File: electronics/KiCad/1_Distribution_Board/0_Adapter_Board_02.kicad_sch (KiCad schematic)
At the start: 16 parts, among them J7 JST PH, J8 Generic 2.54mm

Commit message: footprint additions
Added Footprints to resistors and most components.
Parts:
- R1, R36, R38, R47, R5, R6, R7, R8, R9: footprint (none) -> Resistor_SMD:R_0805_2012Metric_Pad1.20x1.40mm_HandSolder
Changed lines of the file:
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@@
 			)
 		)
-		(property "Footprint" ""
+		(property "Footprint" "Resistor_SMD:R_0805_2012Metric_Pad1.20x1.40mm_HandSolder"
 			(at 41.656 65.024 90)
 			(effects
@@
 			)
 		)
-		(property "Footprint" ""
+		(property "Footprint" "Resistor_SMD:R_0805_2012Metric_Pad1.20x1.40mm_HandSolder"
 			(at 196.596 98.044 90)
 			(effects
@@
 			)
 		)
-		(property "Footprint" ""
+		(property "Footprint" "Resistor_SMD:R_0805_2012Metric_Pad1.20x1.40mm_HandSolder"
 			(at 63.246 65.024 90)
 			(effects
@@
 			)
 		)
-		(property "Footprint" ""
+		(property "Footprint" "Resistor_SMD:R_0805_2012Metric_Pad1.20x1.40mm_HandSolder"
 			(at 60.706 161.544 90)
 			(effects
@@
 			)
 		)
-		(property "Footprint" ""
+		(property "Footprint" "Resistor_SMD:R_0805_2012Metric_Pad1.20x1.40mm_HandSolder"
 			(at 63.246 75.184 90)
 			(effects
@@
 			)
 		)
-		(property "Footprint" ""
+		(property "Footprint" "Resistor_SMD:R_0805_2012Metric_Pad1.20x1.40mm_HandSolder"
 			(at 73.406 26.924 90)
 			(effects
@@
 			)
 		)
-		(property "Footprint" ""
+		(property "Footprint" "Resistor_SMD:R_0805_2012Metric_Pad1.20x1.40mm_HandSolder"
 			(at 72.136 128.524 90)
 			(effects
@@
 			)
 		)
-		(property "Footprint" ""
+		(property "Footprint" "Resistor_SMD:R_0805_2012Metric_Pad1.20x1.40mm_HandSolder"
 			(at 196.596 87.884 90)
 			(effects
@@
 			)
 		)
-		(property "Footprint" ""
+		(property "Footprint" "Resistor_SMD:R_0805_2012Metric_Pad1.20x1.40mm_HandSolder"
 			(at 41.656 75.184 90)
 			(effects

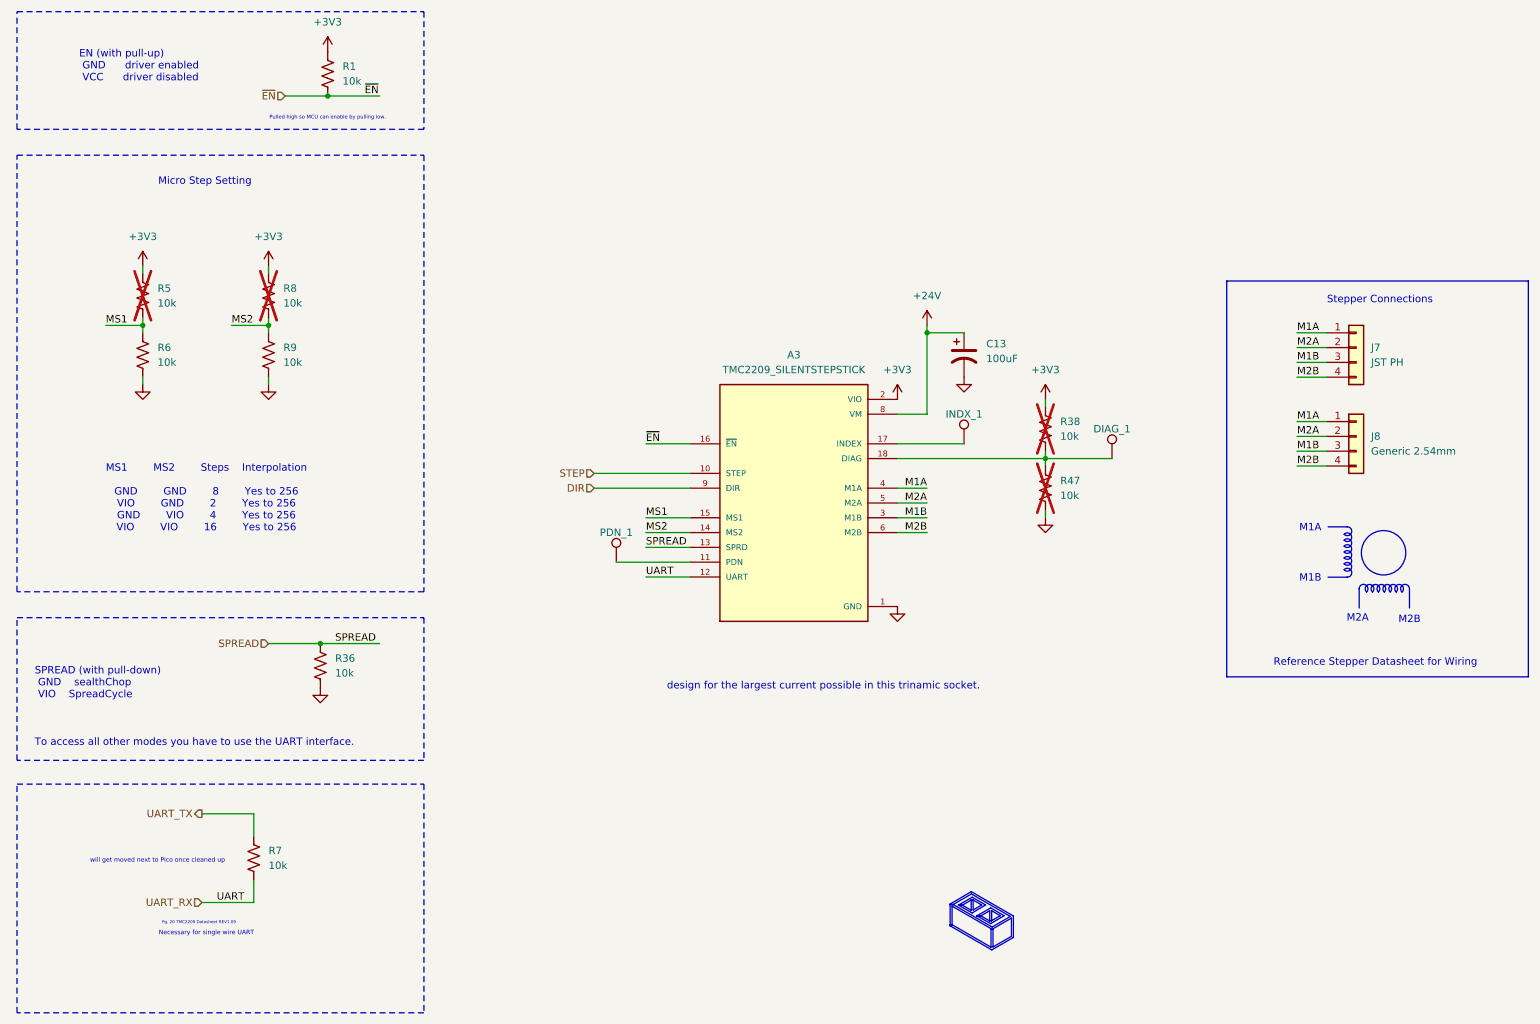
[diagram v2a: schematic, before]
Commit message: Updated to add 2 more steppers
Updated to add two more steppers, dual with the motor controllers. they will be either or. Layout hole pattern started. Still need some footprints assigned.
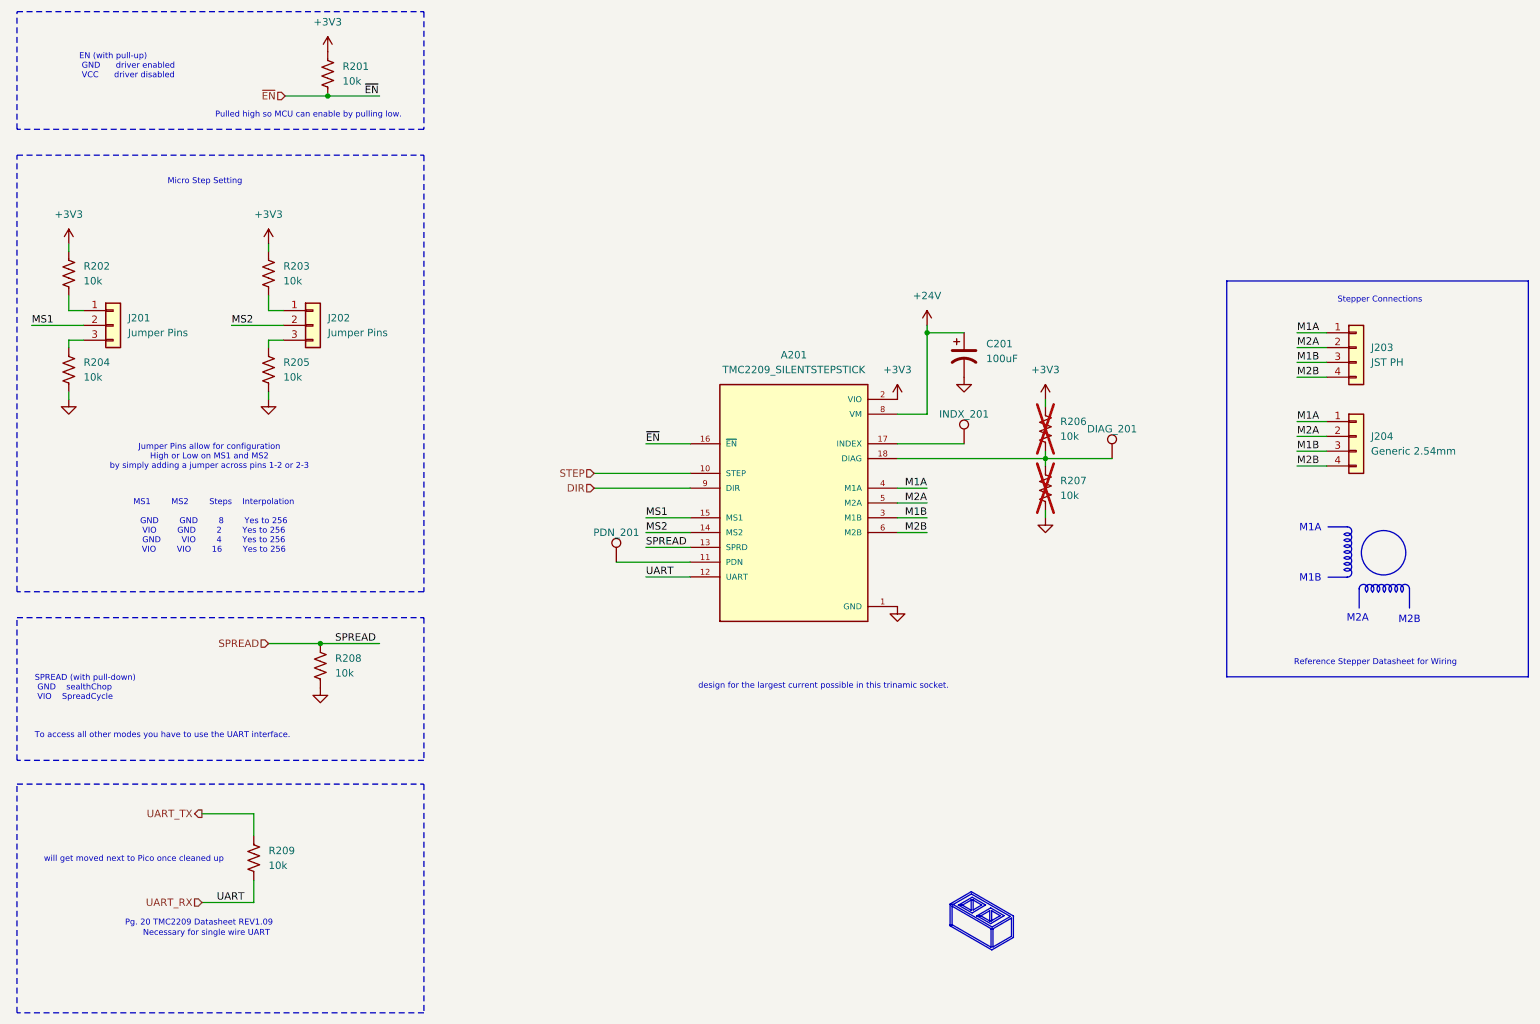
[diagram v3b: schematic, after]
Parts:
- added J201, J202: Jumper Pins, Connector_PinHeader_2.54mm:PinHeader_1x03_P2.54mm_Vertical, symbol Connector_Generic:Conn_01x03
- R202: renamed from R5; now fitted
- R203: renamed from R8; now fitted
- renumbered A3 to A201, C13 to C201, DIAG_1 to DIAG_201, INDX_1 to INDX_201, J7 to J203, J8 to J204, PDN_1 to PDN_201, R1 to R201, R6 to R204, R9 to R205, R38 to R206, R47 to R207, R36 to R208, R7 to R209
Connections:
- net MS1: now also J201.2 (Pin_2); no longer R202.2, R204.1
- net MS2: now also J202.2 (Pin_2); no longer R203.2, R205.1
- new net: J202.1 (Pin_1), R203.2
- new net: J202.3 (Pin_3), R205.1
- new net: J201.1 (Pin_1), R202.2
- new net: J201.3 (Pin_3), R204.1
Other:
- note added: "Jumper Pins allow for configuration High or Low on MS1 and MS2 by simply adding a jumper across pins 1-2 or 2-3"
- moved on the sheet: R204, R205

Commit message: Added 4th stepper
Added 4th stepper on SCH and PCB
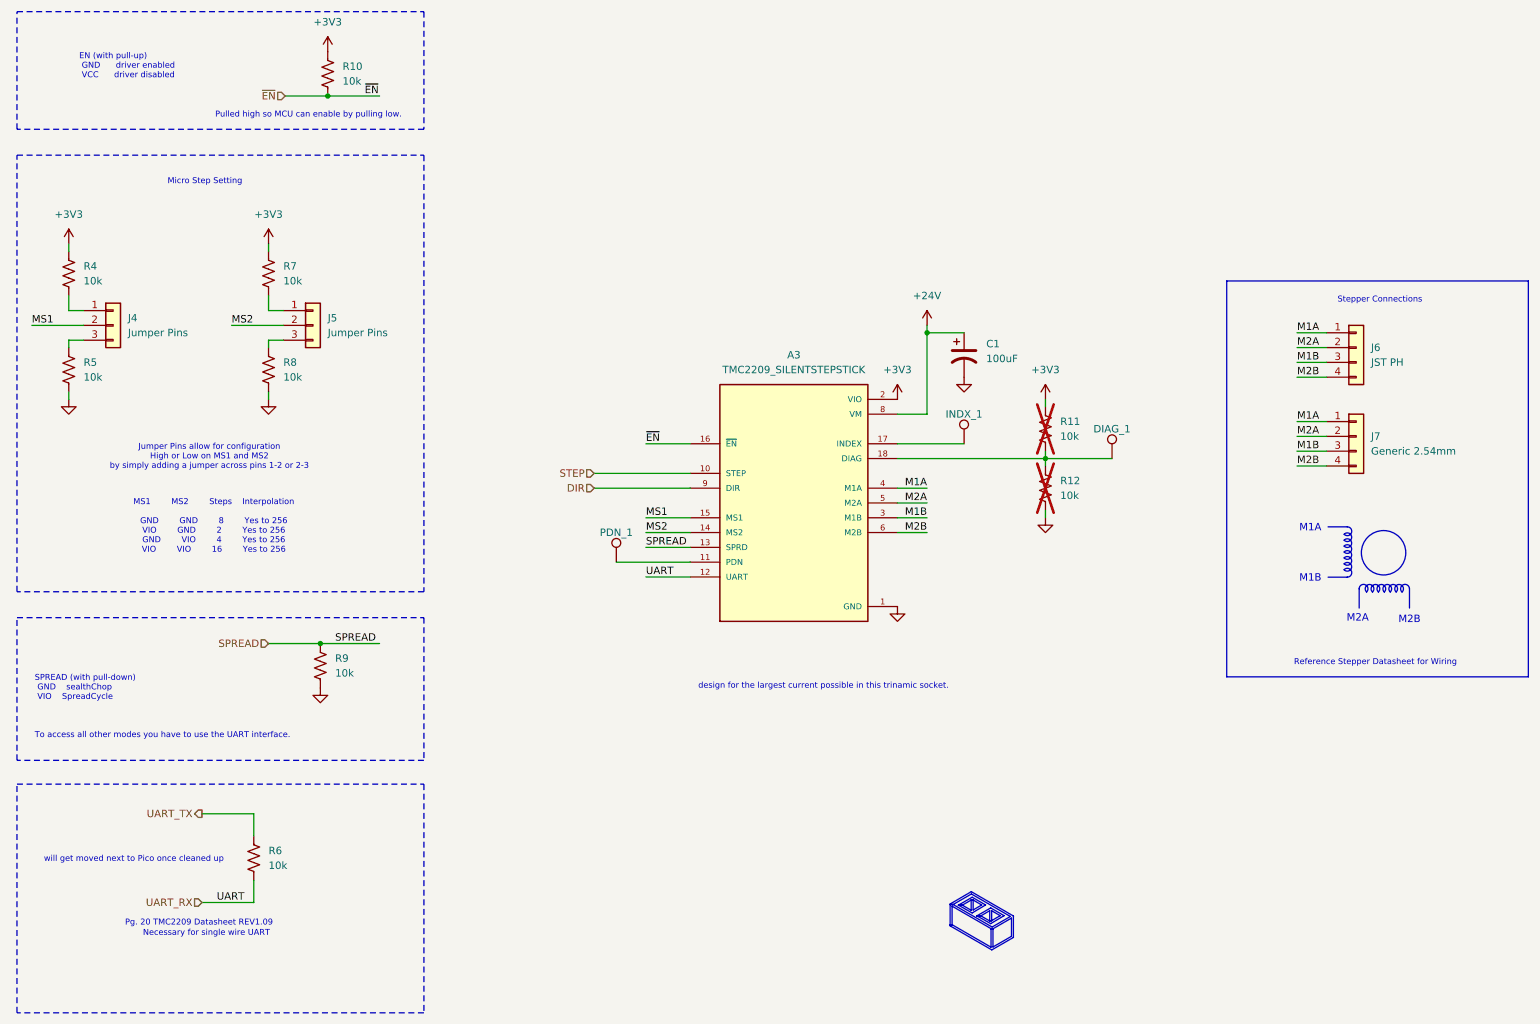
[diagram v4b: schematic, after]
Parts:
- renumbered A201 to A3, C201 to C1, DIAG_201 to DIAG_1, INDX_201 to INDX_1, J201 to J4, J202 to J5, J203 to J6, J204 to J7, PDN_201 to PDN_1, R201 to R10, R206 to R11, R207 to R12, R202 to R4, R204 to R5, R209 to R6, R203 to R7, R205 to R8, R208 to R9

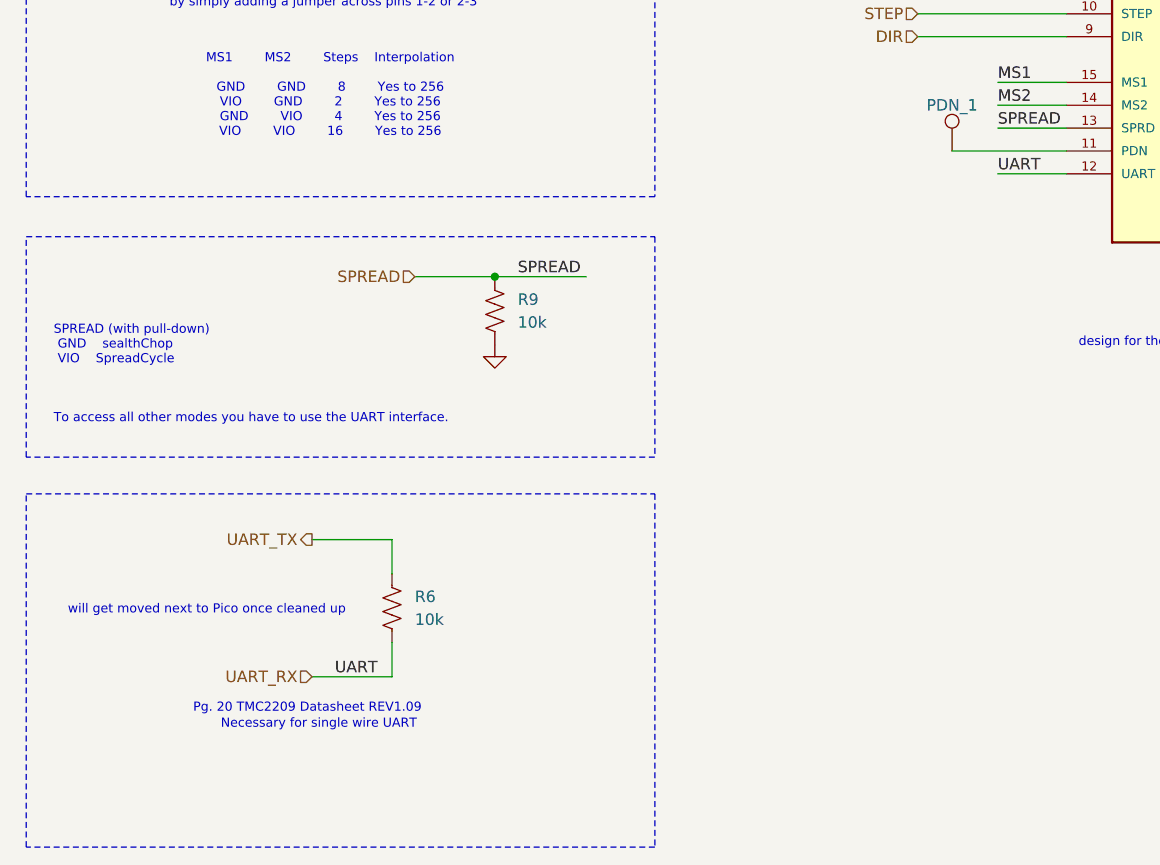
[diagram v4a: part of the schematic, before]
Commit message: Updated Schematics
Corrected Schematics to pull duplicates on the design.
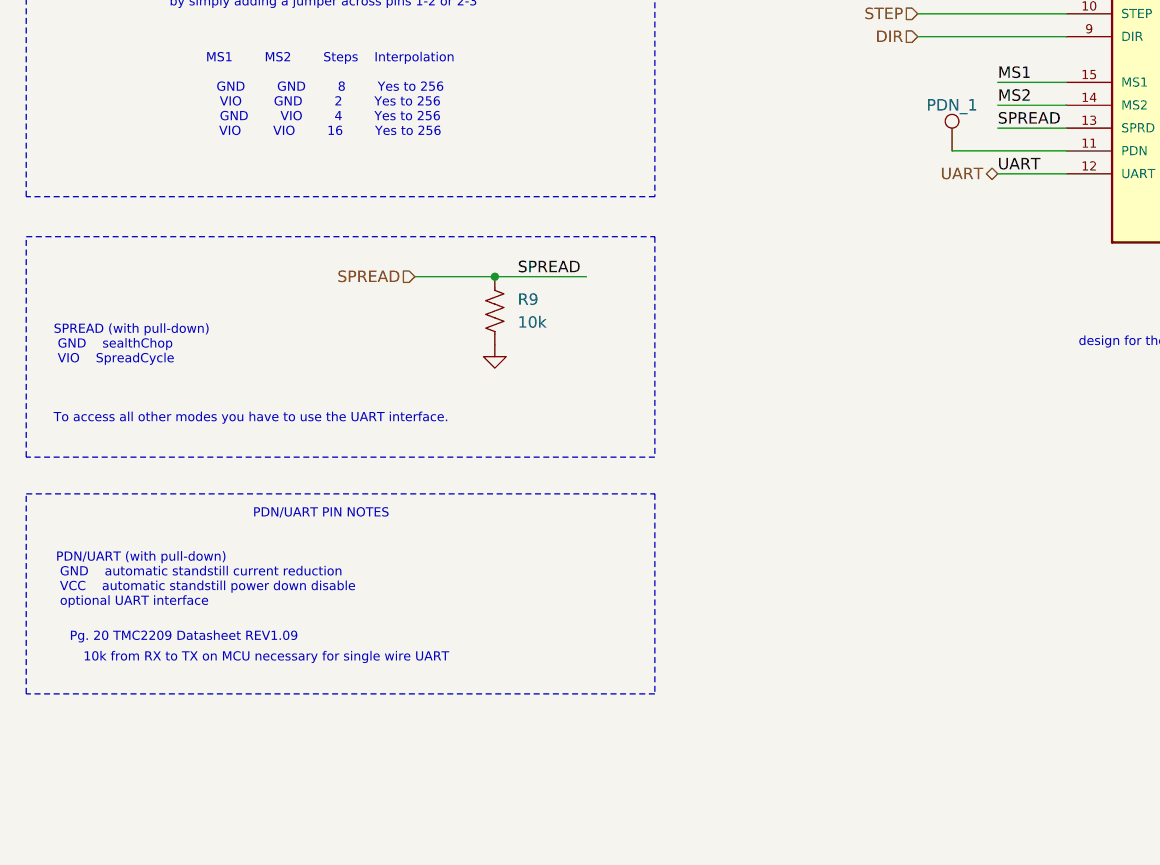
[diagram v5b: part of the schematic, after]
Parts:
- removed R6: 10k, Resistor_SMD:R_0805_2012Metric_Pad1.20x1.40mm_HandSolder, symbol Device:R_US
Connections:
- net UART_RX renamed UART
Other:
- note added: "10k from RX to TX on MCU necessary for single wire UART"
- note added: "PDN/UART (with pull-down) GND automatic standstill current reduction VCC automatic standstill power down disable optional UART interface"
- note added: "PDN/UART PIN NOTES"
- note removed: "Necessary for single wire UART"
- note removed: "will get moved next to Pico once cleaned up"
